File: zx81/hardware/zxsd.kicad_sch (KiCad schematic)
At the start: 36 parts, among them J1 Micro_SD_Card, J2 ZX81_EXP, SW1 RESET, U1 74HCT32, U10 27C256, U11 KM62256CLP, U12 74HCT08, U2 74HCT32, U3 74HCT00, U4 74HCT04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

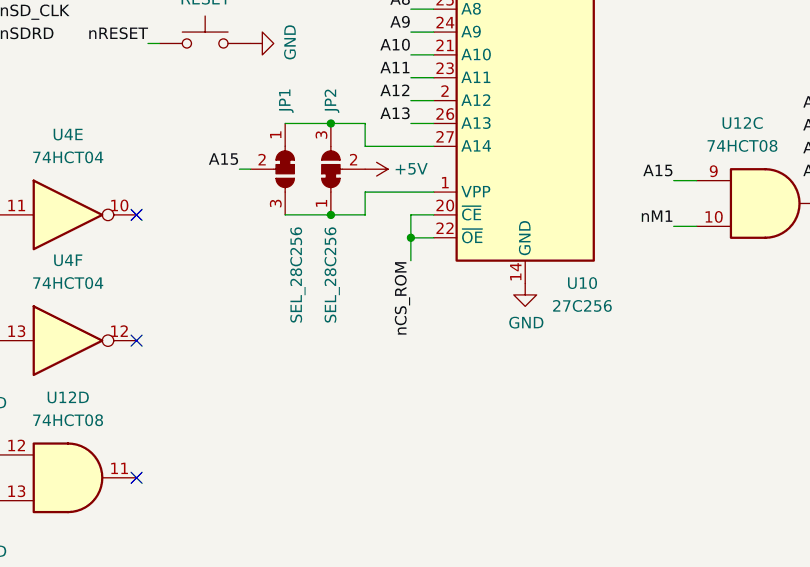
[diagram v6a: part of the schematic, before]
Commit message: tied ROM CE to GND, only use CE (better timing)
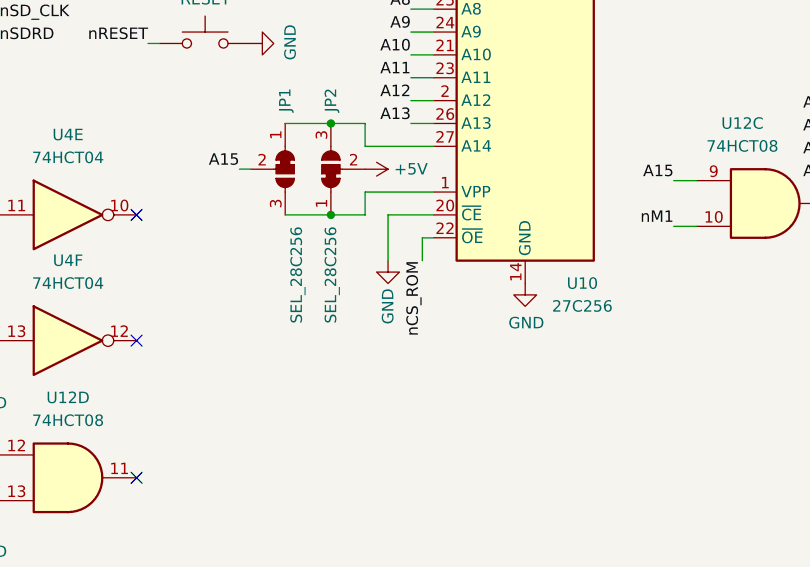
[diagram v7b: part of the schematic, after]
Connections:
- net GND: now also U10.20 (~{CE})
- net nCS_ROM: no longer U10.20 (~{CE})
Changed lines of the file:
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@@
   (junction (at 257.81 106.68) (diameter 0) (color 0 0 0 0)
   )
-  (junction (at 195.58 152.4) (diameter 0) (color 0 0 0 0)
-  )
   (junction (at 30.48 101.6) (diameter 0) (color 0 0 0 0)
   )
@@
     (stroke (width 0) (type default) (color 0 0 0 0))
   )
-  (wire (pts (xy 198.12 149.86) (xy 195.58 149.86))
-    (stroke (width 0) (type default) (color 0 0 0 0))
-  )
   (wire (pts (xy 199.39 21.59) (xy 194.31 21.59))
     (stroke (width 0) (type default) (color 0 0 0 0))
@@
     (stroke (width 0) (type default) (color 0 0 0 0))
   )
+  (wire (pts (xy 196.85 152.4) (xy 198.12 152.4))
+    (stroke (width 0) (type default) (color 0 0 0 0))
+  )
   (wire (pts (xy 194.31 21.59) (xy 189.23 21.59))
     (stroke (width 0) (type default) (color 0 0 0 0))
@@
     (stroke (width 0) (type default) (color 0 0 0 0))
   )
-  (wire (pts (xy 195.58 149.86) (xy 195.58 152.4))
-    (stroke (width 0) (type default) (color 0 0 0 0))
-  )
   (wire (pts (xy 245.11 123.19) (xy 242.57 123.19))
     (stroke (width 0) (type default) (color 0 0 0 0))
@@
     (stroke (width 0) (type default) (color 0 0 0 0))
   )
+  (wire (pts (xy 193.04 149.86) (xy 193.04 154.94))
+    (stroke (width 0) (type default) (color 0 0 0 0))
+  )
   (wire (pts (xy 207.01 44.45) (xy 177.8 44.45))
     (stroke (width 0) (type default) (color 0 0 0 0))
@@
     (stroke (width 0) (type default) (color 0 0 0 0))
   )
-  (wire (pts (xy 195.58 154.94) (xy 195.58 152.4))
-    (stroke (width 0) (type default) (color 0 0 0 0))
-  )
   (wire (pts (xy 198.12 132.08) (xy 195.58 132.08))
     (stroke (width 0) (type default) (color 0 0 0 0))
@@
     (stroke (width 0) (type default) (color 0 0 0 0))
   )
+  (wire (pts (xy 196.85 152.4) (xy 196.85 154.94))
+    (stroke (width 0) (type default) (color 0 0 0 0))
+  )
   (wire (pts (xy 245.11 138.43) (xy 242.57 138.43))
     (stroke (width 0) (type default) (color 0 0 0 0))
@@
     (stroke (width 0) (type default) (color 0 0 0 0))
   )
-  (wire (pts (xy 195.58 152.4) (xy 198.12 152.4))
+  (wire (pts (xy 121.92 57.15) (xy 119.38 57.15))
     (stroke (width 0) (type default) (color 0 0 0 0))
   )
-  (wire (pts (xy 121.92 57.15) (xy 119.38 57.15))
+  (wire (pts (xy 198.12 149.86) (xy 193.04 149.86))
     (stroke (width 0) (type default) (color 0 0 0 0))
   )
@@
     (effects (font (size 1.27 1.27)) (justify left bottom))
   )
-  (label "nCS_ROM" (at 195.58 154.94 270)
+  (label "nCS_ROM" (at 196.85 154.94 270)
     (effects (font (size 1.27 1.27)) (justify right bottom))
   )
@@
     (pin "1")
   )
+  (symbol (lib_id "power:GND") (at 193.04 154.94 0) (unit 1)
+    (in_bom yes) (on_board yes)
+    (property "Reference" "#PWR?" (id 0) (at 193.04 161.29 0)
+      (effects (font (size 1.27 1.27)) hide)
+    )
+    (property "Value" "GND" (id 1) (at 193.04 160.02 90))
+    (property "Footprint" "" (id 2) (at 193.04 154.94 0)
+      (effects (font (size 1.27 1.27)) hide)
+    )
+    (property "Datasheet" "" (id 3) (at 193.04 154.94 0)
+      (effects (font (size 1.27 1.27)) hide)
+    )
+    (pin "1")
+  )
   (symbol (lib_id "Regulator_Linear:MCP1700x-330xxTO") (at 86.36 49.53 0) (mirror x) (unit 1)
     (in_bom yes) (on_board yes) (fields_autoplaced)
@@
       (reference "#PWR0127") (unit 1) (value "+3.3V") (footprint "")
     )
+    (path "/ba6f9c95-ca6f-4eb9-8074-0942ae88df92"
+      (reference "#PWR?") (unit 1) (value "GND") (footprint "")
+    )
     (path "/00000000-0000-0000-0000-000061e15748"

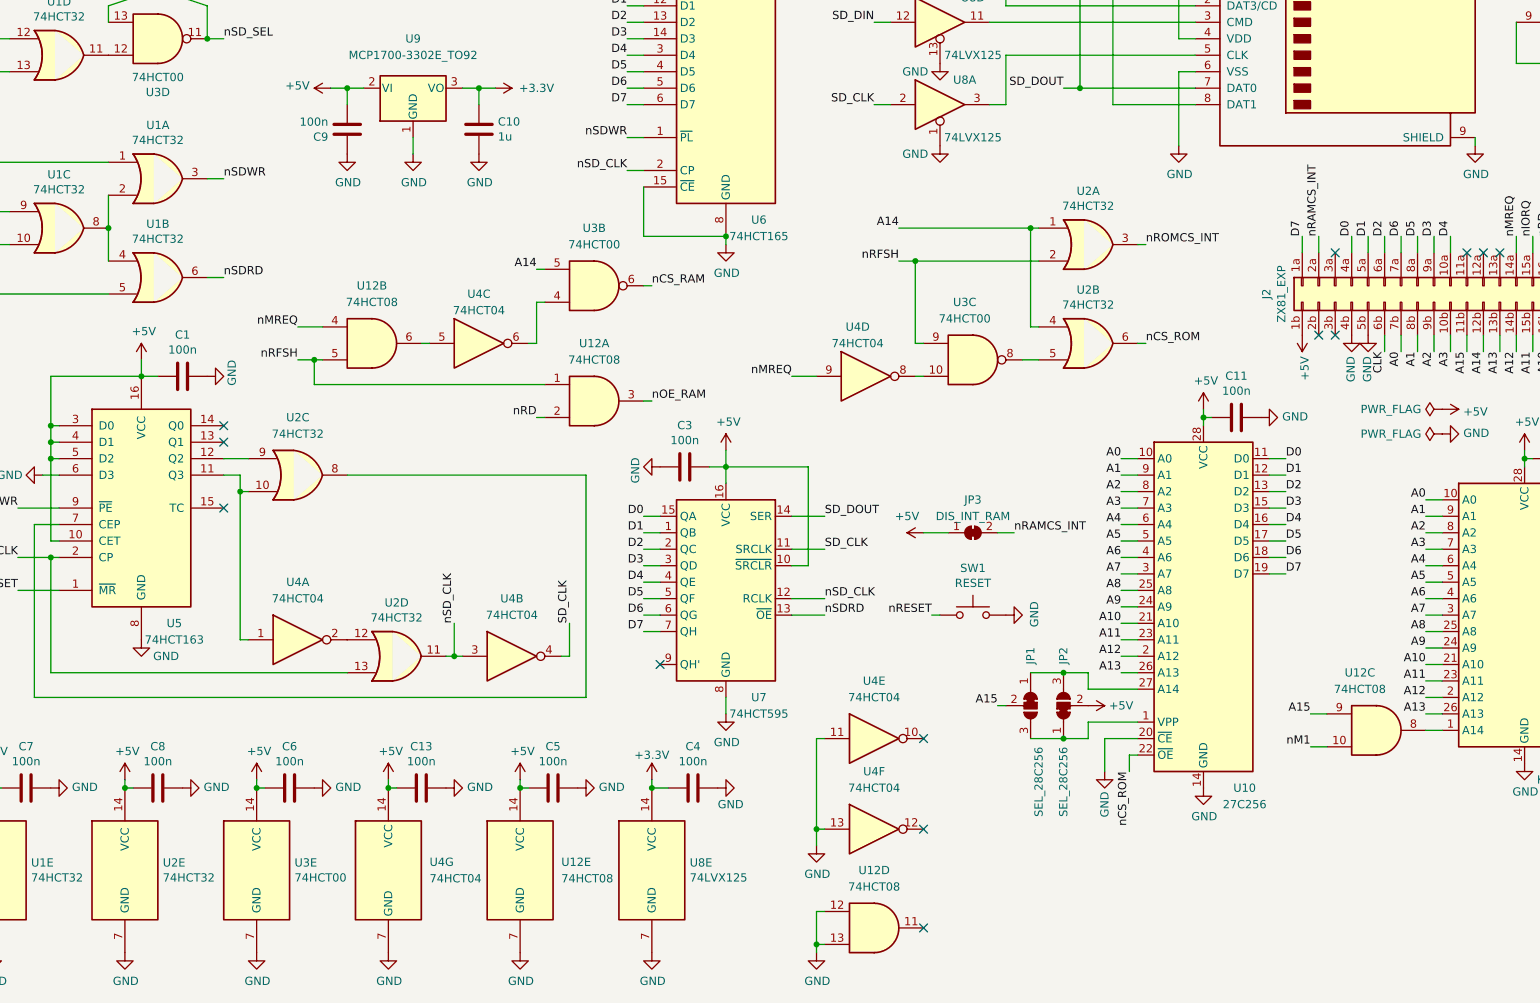
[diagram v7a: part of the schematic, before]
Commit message: full decoder logic finished
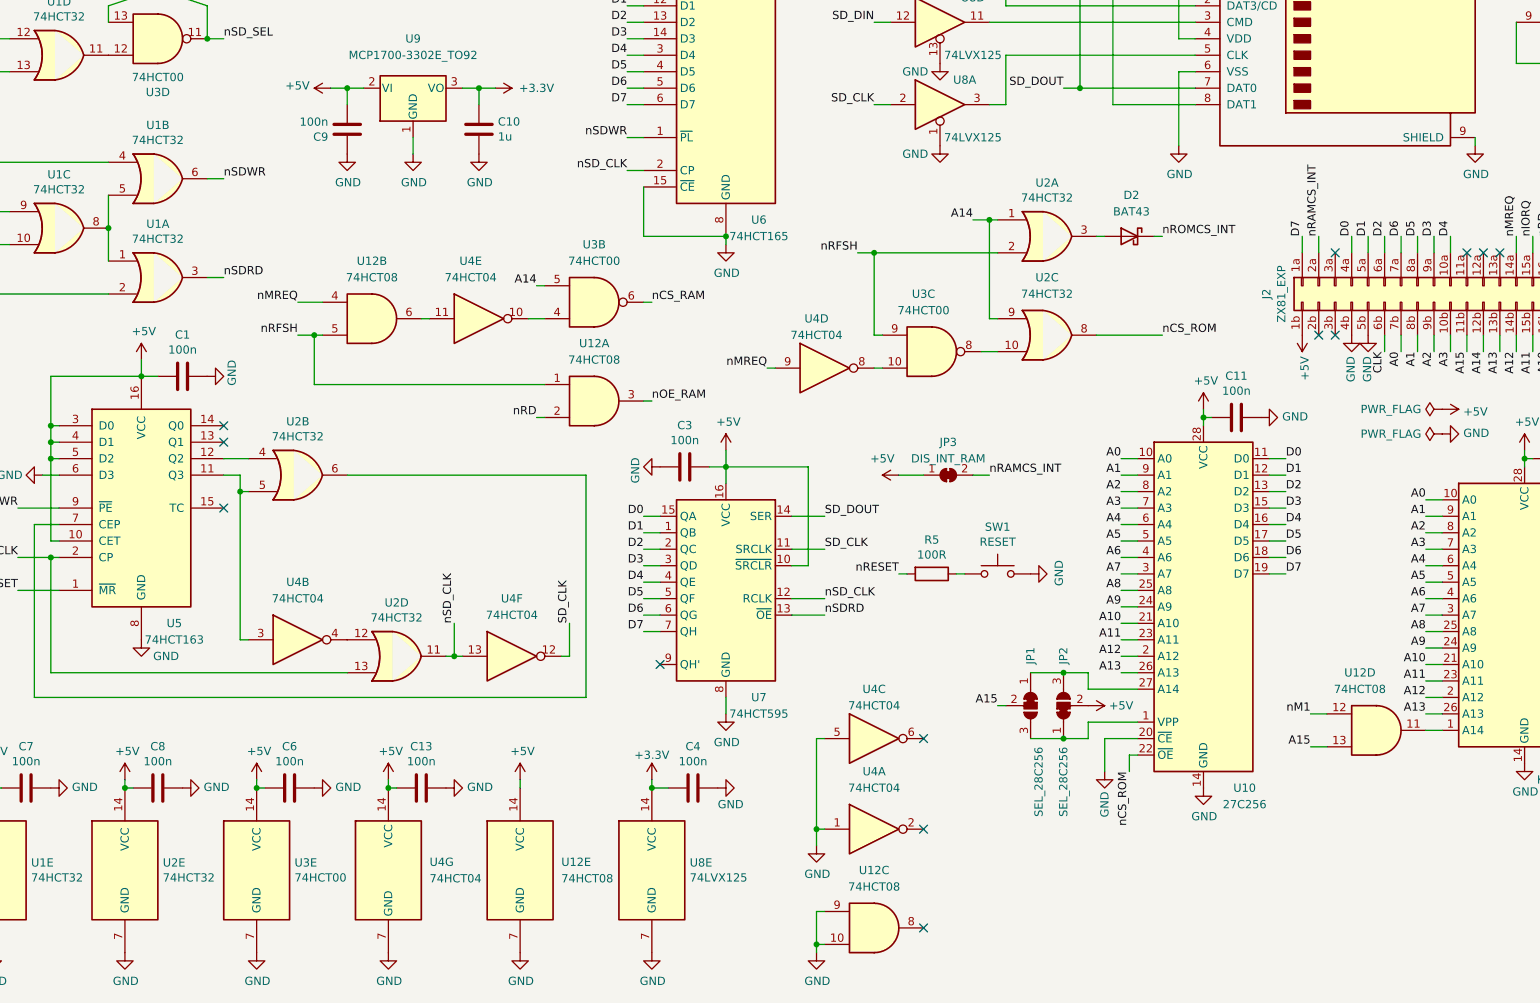
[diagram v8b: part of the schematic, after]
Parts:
- removed C5: 100n, Capacitor_THT:C_Disc_D5.0mm_W2.5mm_P5.00mm, symbol Device:C
- added D2: BAT43, Diode_THT:D_DO-35_SOD27_P2.54mm_Vertical_AnodeUp, symbol Diode:BAT43
- added R5: 100R, Resistor_THT:R_Axial_DIN0207_L6.3mm_D2.5mm_P10.16mm_Horizontal, symbol Device:R
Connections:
- net A14: now also U2.9; no longer U2.4
- net A15: now also U12.13; no longer U12.9
- net GND: now also U12.10, U12.9, U4.1, U4.5; no longer U12.12, U12.13, U4.11, U4.13
- net SD_CLK: now also U4.12; no longer U4.4
- net nCS_ROM: now also U2.8; no longer U2.6
- net nM1: now also U12.12; no longer U12.10
- net nRD: now also U1.2; no longer U1.5
- net nRESET: now also R5.2; no longer SW1.1
- net nROMCS_INT: now also D2.1 (K); no longer U2.3
- net nSDRD: now also U1.3; no longer U1.6
- net nSDWR: now also U1.6; no longer U1.3
- net nSD_CLK: now also U4.13; no longer U4.3
- net nWR: now also U1.4; no longer U1.1
- net at U11.1 (A14): now also U12.11; no longer U12.8
- net at U5.12 (Q2): now also U2.4; no longer U2.9
- net at U5.7 (CEP): now also U2.6; no longer U2.8
- net at U2.5: now also U4.3, U5.11 (Q3); no longer U3.8
- net at U3.4: now also U4.10; no longer U4.6
- net at U2.12: now also U4.4; no longer U4.2
- net at U12.6: now also U4.11; no longer U4.5
- new net: U1.1, U1.5, U1.8
- new net: U2.10, U3.8
- new net: R5.1, SW1.1
- new net: D2.2 (A), U2.3
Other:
- moved on the sheet: JP3, SW1, U12B, U12C, U12D, U1A, U1B, U2A, U2B, U2C, U3B, U3C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
